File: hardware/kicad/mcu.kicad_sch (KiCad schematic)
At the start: 10 parts, among them CN1 OLED_SSD1306_I2C, SW1 RESET, SW2 BOOT, U6 ESP32-S3-WROOM-1-N16R8

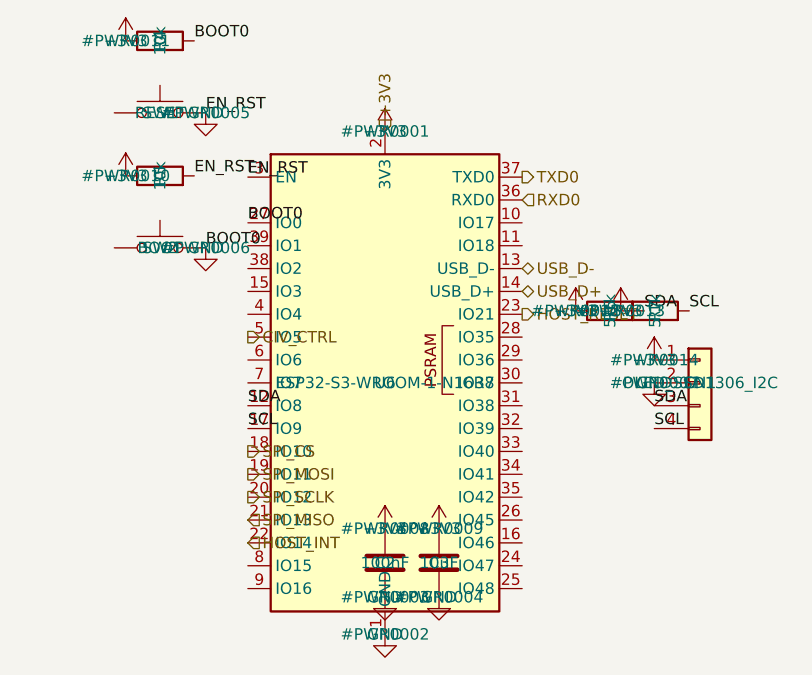
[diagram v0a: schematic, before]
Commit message: fix: repair schematic connectivity, real MAX3421E pinout, footprint assignment
- Root sheet pins were placed outside the sheet boxes, so no cross-sheet
  net (IO5->CI-V, USB D+/D-, SPI, VBUS_5V, 5V_HOST) was actually connected.
  Rebuilt pins on the sheet borders with wire stubs + labels.
- MCU: SW1/SW2 pin 2 carried both GND and EN/BOOT0 (short to ground);
  GND moved to pin 1. Unused ESP32 GPIOs marked no-connect.
- USB_Host rebuilt around the real MAX3421E TQFN-32 pinout (datasheet
  19-3953): 33 ohm D+/D- series resistors, 1uF VCC/VBCOMP, 0.1uF VL.
- J1 now AudioJack3 (T/R/S) with CUI SJ1-3523N footprint; Q1 is a real
  2N7000 (TO-92).
- PWR_FLAGs added; ERC (raw kicad-cli) has 0 errors.
- Board outline 65x45 mm, 54 footprints assigned and written to symbol
  Footprint fields, netlist applied. Placement is a rough grid only; no
  routing yet.
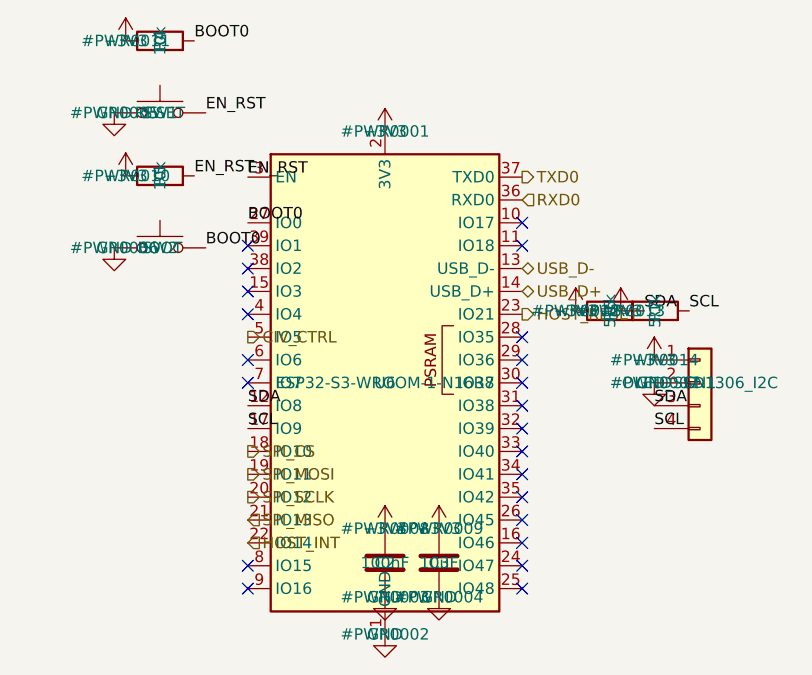
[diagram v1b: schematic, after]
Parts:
- C2, C3: footprint (none) -> Capacitor_SMD:C_0603_1608Metric
- CN1: footprint (none) -> Connector_JST:JST_PH_B4B-PH-K_1x04_P2.00mm_Vertical
- R4, R5, R6, R7: footprint (none) -> Resistor_SMD:R_0603_1608Metric
- SW1, SW2: footprint (none) -> Button_Switch_SMD:SW_SPST_B3S-1000
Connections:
- net GND: now also SW1.1, SW2.1; no longer R4.2, R5.2, SW1.2, SW2.2, U6.27 (IO0), U6.3 (EN)
- new net BOOT0: R4.2, SW2.2, U6.27 (IO0)
- new net EN_RST: R5.2, SW1.2, U6.3 (EN)
- no-connect marks 0 -> 22
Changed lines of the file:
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@@
 			)
 		)
-		(property "Footprint" ""
+		(property "Footprint" "Button_Switch_SMD:SW_SPST_B3S-1000"
 			(at 15 80 0)
 			(effects
@@
 			)
 		)
-		(property "Footprint" ""
+		(property "Footprint" "Button_Switch_SMD:SW_SPST_B3S-1000"
 			(at 15 95 0)
 			(effects
@@
 			)
 		)
-		(property "Footprint" ""
+		(property "Footprint" "Resistor_SMD:R_0603_1608Metric"
 			(at 15 72 0)
 			(effects
@@
 			)
 		)
-		(property "Footprint" ""
+		(property "Footprint" "Resistor_SMD:R_0603_1608Metric"
 			(at 15 87 0)
 			(effects
@@
 			)
 		)
-		(property "Footprint" ""
+		(property "Footprint" "Connector_JST:JST_PH_B4B-PH-K_1x04_P2.00mm_Vertical"
 			(at 75 110 0)
 			(effects
@@
 			)
 		)
-		(property "Footprint" ""
+		(property "Footprint" "Resistor_SMD:R_0603_1608Metric"
 			(at 65 102 0)
 			(effects
@@
 			)
 		)
-		(property "Footprint" ""
+		(property "Footprint" "Resistor_SMD:R_0603_1608Metric"
 			(at 70 102 0)
 			(effects
@@
 			)
 		)
-		(property "Footprint" ""
+		(property "Footprint" "Capacitor_SMD:C_0603_1608Metric"
 			(at 40 130 0)
 			(effects
@@
 			)
 		)
-		(property "Footprint" ""
+		(property "Footprint" "Capacitor_SMD:C_0603_1608Metric"
 			(at 46 130 0)
 			(effects
@@
 				(path "/840e083b-e0fc-4c92-9ef6-5f402d7ae31c/8057cc52-6c91-402d-afb6-e804030a5d01"
 					(reference "#PWR0004")
-					(unit 1)
-				)
-			)
-		)
-	)
-	(symbol
-		(lib_id "power:GND")
-		(at 20.08 80 0)
-		(unit 1)
-		(exclude_from_sim no)
-		(in_bom yes)
-		(on_board yes)
-		(dnp no)
-		(property "Reference" "#PWR0005"
-			(at 20.08 80 0)
-			(effects
-				(font
-					(size 1.27 1.27)
-				)
-			)
-		)
-		(property "Value" "GND"
-			(at 20.08 80 0)
-			(effects
-				(font
-					(size 1.27 1.27)
-				)
-			)
-		)
-		(property "Footprint" ""
-			(at 20.08 80 0)
-			(effects
-				(font
-					(size 1.27 1.27)
-				)
-				(hide yes)
-			)
-		)
-		(property "Datasheet" ""
-			(at 20.08 80 0)
-			(effects
-				(font
-					(size 1.27 1.27)
-				)
-				(hide yes)
-			)
-		)
-		(property "Description" "Power symbol creates a global label with name \"GND\" , ground"
-			(at 20.08 80 0)
-			(effects
-				(font
-					(size 1.27 1.27)
-				)
-				(hide yes)
-			)
-		)
-		(pin "1"
-		)
-		(instances
-			(project "WaveRig"
-				(path "/840e083b-e0fc-4c92-9ef6-5f402d7ae31c/8057cc52-6c91-402d-afb6-e804030a5d01"
-					(reference "#PWR0005")
-					(unit 1)
-				)
-			)
-		)
-	)
-	(symbol
-		(lib_id "power:GND")
-		(at 20.08 95 0)
-		(unit 1)
-		(exclude_from_sim no)
-		(in_bom yes)
-		(on_board yes)
-		(dnp no)
-		(property "Reference" "#PWR0006"
-			(at 20.08 95 0)
-			(effects
-				(font
-					(size 1.27 1.27)
-				)
-			)
-		)
-		(property "Value" "GND"
-			(at 20.08 95 0)
-			(effects
-				(font
-					(size 1.27 1.27)
-				)
-			)
-		)
-		(property "Footprint" ""
-			(at 20.08 95 0)
-			(effects
-				(font
-					(size 1.27 1.27)
-				)
-				(hide yes)
-			)
-		)
-		(property "Datasheet" ""
-			(at 20.08 95 0)
-			(effects
-				(font
-					(size 1.27 1.27)
-				)
-				(hide yes)
-			)
-		)
-		(property "Description" "Power symbol creates a global label with name \"GND\" , ground"
-			(at 20.08 95 0)
-			(effects
-				(font
-					(size 1.27 1.27)
-				)
-				(hide yes)
-			)
-		)
-		(pin "1"
-		)
-		(instances
-			(project "WaveRig"
-				(path "/840e083b-e0fc-4c92-9ef6-5f402d7ae31c/8057cc52-6c91-402d-afb6-e804030a5d01"
-					(reference "#PWR0006")
 					(unit 1)
 				)
@@
 		)
 	)
-	(hierarchical_label "+3V3"
-		(shape input)
-		(at 40 82.06 90)
-		(effects
-			(font
-				(size 1.27 1.27)
-			)
-			(justify left)
-		)
+	(symbol
+		(lib_id "power:GND")
+		(at 9.92 80 0)
+		(unit 1)
+		(exclude_from_sim no)
+		(in_bom yes)
+		(on_board yes)
+		(dnp no)
+		(property "Reference" "#PWR0005"
+			(at 9.92 80 0)
+			(effects
+				(font
+					(size 1.27 1.27)
+				)
+			)
+		)
+		(property "Value" "GND"
+			(at 9.92 80 0)
+			(effects
+				(font
+					(size 1.27 1.27)
+				)
+			)
+		)
+		(property "Footprint" ""
+			(at 9.92 80 0)
+			(effects
+				(font
+					(size 1.27 1.27)
+				)
+				(hide yes)
+			)
+		)
+		(property "Datasheet" ""
+			(at 9.92 80 0)
+			(effects
+				(font
+					(size 1.27 1.27)
+				)
+				(hide yes)
+			)
+		)
+		(property "Description" "Power symbol creates a global label with name \"GND\" , ground"
+			(at 9.92 80 0)
+			(effects
+				(font
+					(size 1.27 1.27)
+				)
+				(hide yes)
+			)
+		)
+		(pin "1"
+		)
+		(instances
+			(project "WaveRig"
+				(path "/840e083b-e0fc-4c92-9ef6-5f402d7ae31c/8057cc52-6c91-402d-afb6-e804030a5d01"
+					(reference "#PWR0005")
+					(unit 1)
+				)
+			)
+		)
+	)
+	(symbol
+		(lib_id "power:GND")
+		(at 9.92 95 0)
+		(unit 1)
+		(exclude_from_sim no)
+		(in_bom yes)
+		(on_board yes)
+		(dnp no)
+		(property "Reference" "#PWR0006"
+			(at 9.92 95 0)
+			(effects
+				(font
+					(size 1.27 1.27)
+				)
+			)
+		)
+		(property "Value" "GND"
+			(at 9.92 95 0)
+			(effects
+				(font
+					(size 1.27 1.27)
+				)
+			)
+		)
+		(property "Footprint" ""
+			(at 9.92 95 0)
+			(effects
+				(font
+					(size 1.27 1.27)
+				)
+				(hide yes)
+			)
+		)
+		(property "Datasheet" ""
+			(at 9.92 95 0)
+			(effects
+				(font
+					(size 1.27 1.27)
+				)
+				(hide yes)
+			)
+		)
+		(property "Description" "Power symbol creates a global label with name \"GND\" , ground"
+			(at 9.92 95 0)
+			(effects
+				(font
+					(size 1.27 1.27)
+				)
+				(hide yes)
+			)
+		)
+		(pin "1"
+		)
+		(instances
+			(project "WaveRig"
+				(path "/840e083b-e0fc-4c92-9ef6-5f402d7ae31c/8057cc52-6c91-402d-afb6-e804030a5d01"
+					(reference "#PWR0006")
+					(unit 1)
+				)
+			)
+		)
+	)
+	(no_connect
+		(at 24.76 102.38)
+	)
+	(no_connect
+		(at 24.76 107.46)
+	)
+	(no_connect
+		(at 24.76 110)
+	)
+	(no_connect
+		(at 24.76 130.32)
+	)
+	(no_connect
+		(at 24.76 132.86)
+	)
+	(no_connect
+		(at 55.24 92.22)
+	)
+	(no_connect
+		(at 55.24 94.76)
+	)
+	(no_connect
+		(at 24.76 99.84)
+	)
+	(no_connect
+		(at 55.24 127.78)
+	)
+	(no_connect
+		(at 55.24 130.32)
+	)
+	(no_connect
+		(at 55.24 132.86)
+	)
+	(no_connect
+		(at 55.24 125.24)
+	)
+	(no_connect
+		(at 55.24 104.92)
+	)
+	(no_connect
+		(at 55.24 107.46)
+	)
+	(no_connect
+		(at 55.24 110)
+	)
+	(no_connect
+		(at 55.24 112.54)
+	)
+	(no_connect
+		(at 55.24 115.08)
+	)
+	(no_connect
+		(at 55.24 117.62)
+	)
+	(no_connect
+		(at 55.24 120.16)
+	)
+	(no_connect
+		(at 55.24 122.7)
+	)
+	(no_connect
+		(at 24.76 97.3)
+	)
+	(no_connect
+		(at 24.76 94.76)
 	)
 )

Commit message: fix: datasheet audit - correct charger pinout, LDO for 3V3, DW01A/FS8205A, MAX3232, CI-V RX
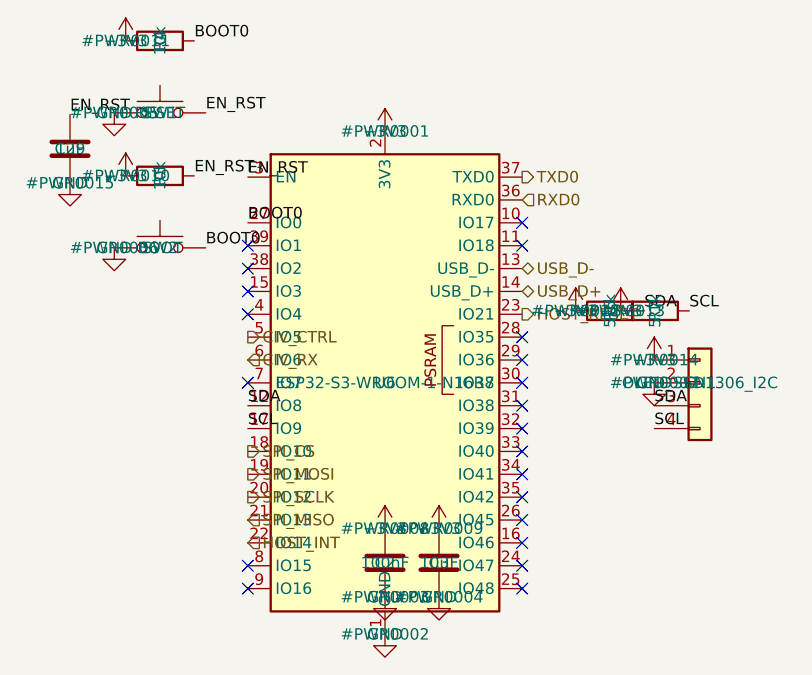
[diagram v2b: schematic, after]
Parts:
- added C29: 1uF, Capacitor_SMD:C_0603_1608Metric, symbol Device:C
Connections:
- net EN_RST: now also C29.1
- net GND: now also C29.2
- net CIV_RX: now reaches U6.6 (IO6)
- no-connect marks 22 -> 21
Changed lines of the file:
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@@
-	)
-	(no_connect
-		(at 24.76 107.46)
 	)
 	(no_connect
@@
 		(at 24.76 94.76)
 	)
+	(symbol
+		(lib_id "Device:C")
+		(at 5 84 0)
+		(unit 1)
+		(exclude_from_sim no)
+		(in_bom yes)
+		(on_board yes)
+		(dnp no)
+		(property "Reference" "C29"
+			(at 5 84 0)
+			(effects
+				(font
+					(size 1.27 1.27)
+				)
+			)
+		)
+		(property "Value" "1uF"
+			(at 5 84 0)
+			(effects
+				(font
+					(size 1.27 1.27)
+				)
+			)
+		)
+		(property "Footprint" "Capacitor_SMD:C_0603_1608Metric"
+			(at 5 84 0)
+			(effects
+				(font
+					(size 1.27 1.27)
+				)
+				(hide yes)
+			)
+		)
+		(property "Datasheet" ""
+			(at 5 84 0)
+			(effects
+				(font
+					(size 1.27 1.27)
+				)
+				(hide yes)
+			)
+		)
+		(property "Description" "Unpolarized capacitor"
+			(at 5 84 0)
+			(effects
+				(font
+					(size 1.27 1.27)
+				)
+				(hide yes)
+			)
+		)
+		(pin "1"
+		)
+		(pin "2"
+		)
+		(instances
+			(project "WaveRig"
+				(path "/840e083b-e0fc-4c92-9ef6-5f402d7ae31c/8057cc52-6c91-402d-afb6-e804030a5d01"
+					(reference "C29")
+					(unit 1)
+				)
+			)
+		)
+	)
+	(label "EN_RST"
+		(at 5 80.19 0)
+		(effects
+			(font
+				(size 1.27 1.27)
+			)
+			(justify left bottom)
+		)
+	)
+	(symbol
+		(lib_id "power:GND")
+		(at 5 87.81 0)
+		(unit 1)
+		(exclude_from_sim no)
+		(in_bom yes)
+		(on_board yes)
+		(dnp no)
+		(property "Reference" "#PWR0015"
+			(at 5 87.81 0)
+			(effects
+				(font
+					(size 1.27 1.27)
+				)
+			)
+		)
+		(property "Value" "GND"
+			(at 5 87.81 0)
+			(effects
+				(font
+					(size 1.27 1.27)
+				)
+			)
+		)
+		(property "Footprint" ""
+			(at 5 87.81 0)
+			(effects
+				(font
+					(size 1.27 1.27)
+				)
+				(hide yes)
+			)
+		)
+		(property "Datasheet" ""
+			(at 5 87.81 0)
+			(effects
+				(font
+					(size 1.27 1.27)
+				)
+				(hide yes)
+			)
+		)
+		(property "Description" "Power symbol creates a global label with name \"GND\" , ground"
+			(at 5 87.81 0)
+			(effects
+				(font
+					(size 1.27 1.27)
+				)
+				(hide yes)
+			)
+		)
+		(pin "1"
+		)
+		(instances
+			(project "WaveRig"
+				(path "/840e083b-e0fc-4c92-9ef6-5f402d7ae31c/8057cc52-6c91-402d-afb6-e804030a5d01"
+					(reference "#PWR0015")
+					(unit 1)
+				)
+			)
+		)
+	)
+	(hierarchical_label "CIV_RX"
+		(shape input)
+		(at 24.76 107.46 180)
+		(effects
+			(font
+				(size 1.27 1.27)
+			)
+			(justify left)
+		)
+	)
 )
